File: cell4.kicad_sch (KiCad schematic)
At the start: 31 parts, among them K4 V23105A5001A201, Q12 IRLML0030, Q13 IRLML0030, SW8 SW_SPST, SW9 SW_SPST, U3 LMV324

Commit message: cell changes and fixes
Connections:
- net Batt+: now also C38.1, R62.2; no longer C39.1, R63.2
- net Batt-: now also C39.1, R63.2; no longer C38.1, R62.2
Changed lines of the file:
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@@
 	(hierarchical_label "Batt-"
 		(shape input)
-		(at 238.125 126.365 0)
+		(at 238.125 146.05 0)
 		(effects
 			(font
@@
 	(hierarchical_label "Batt+"
 		(shape input)
-		(at 238.125 146.05 0)
+		(at 238.125 126.365 0)
 		(effects
 			(font

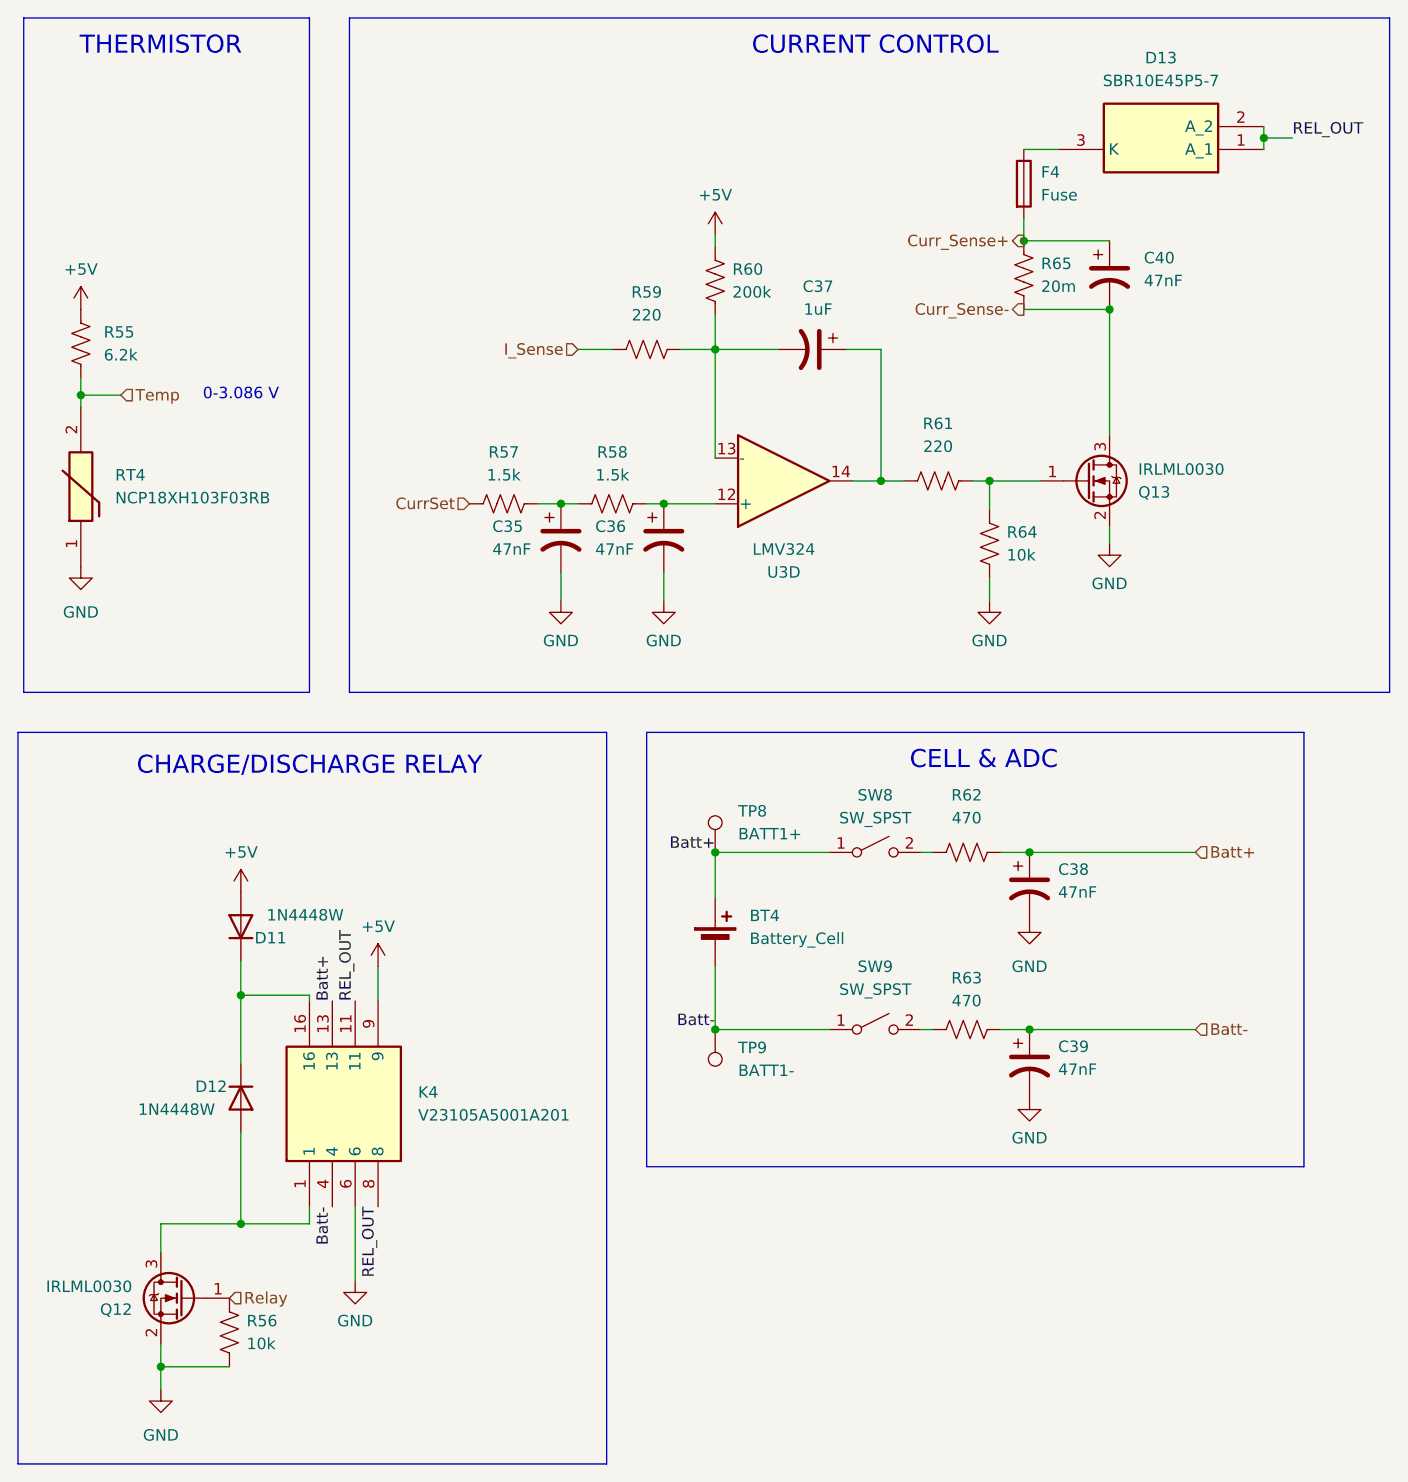
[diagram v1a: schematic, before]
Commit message: Updated current control loop hardware
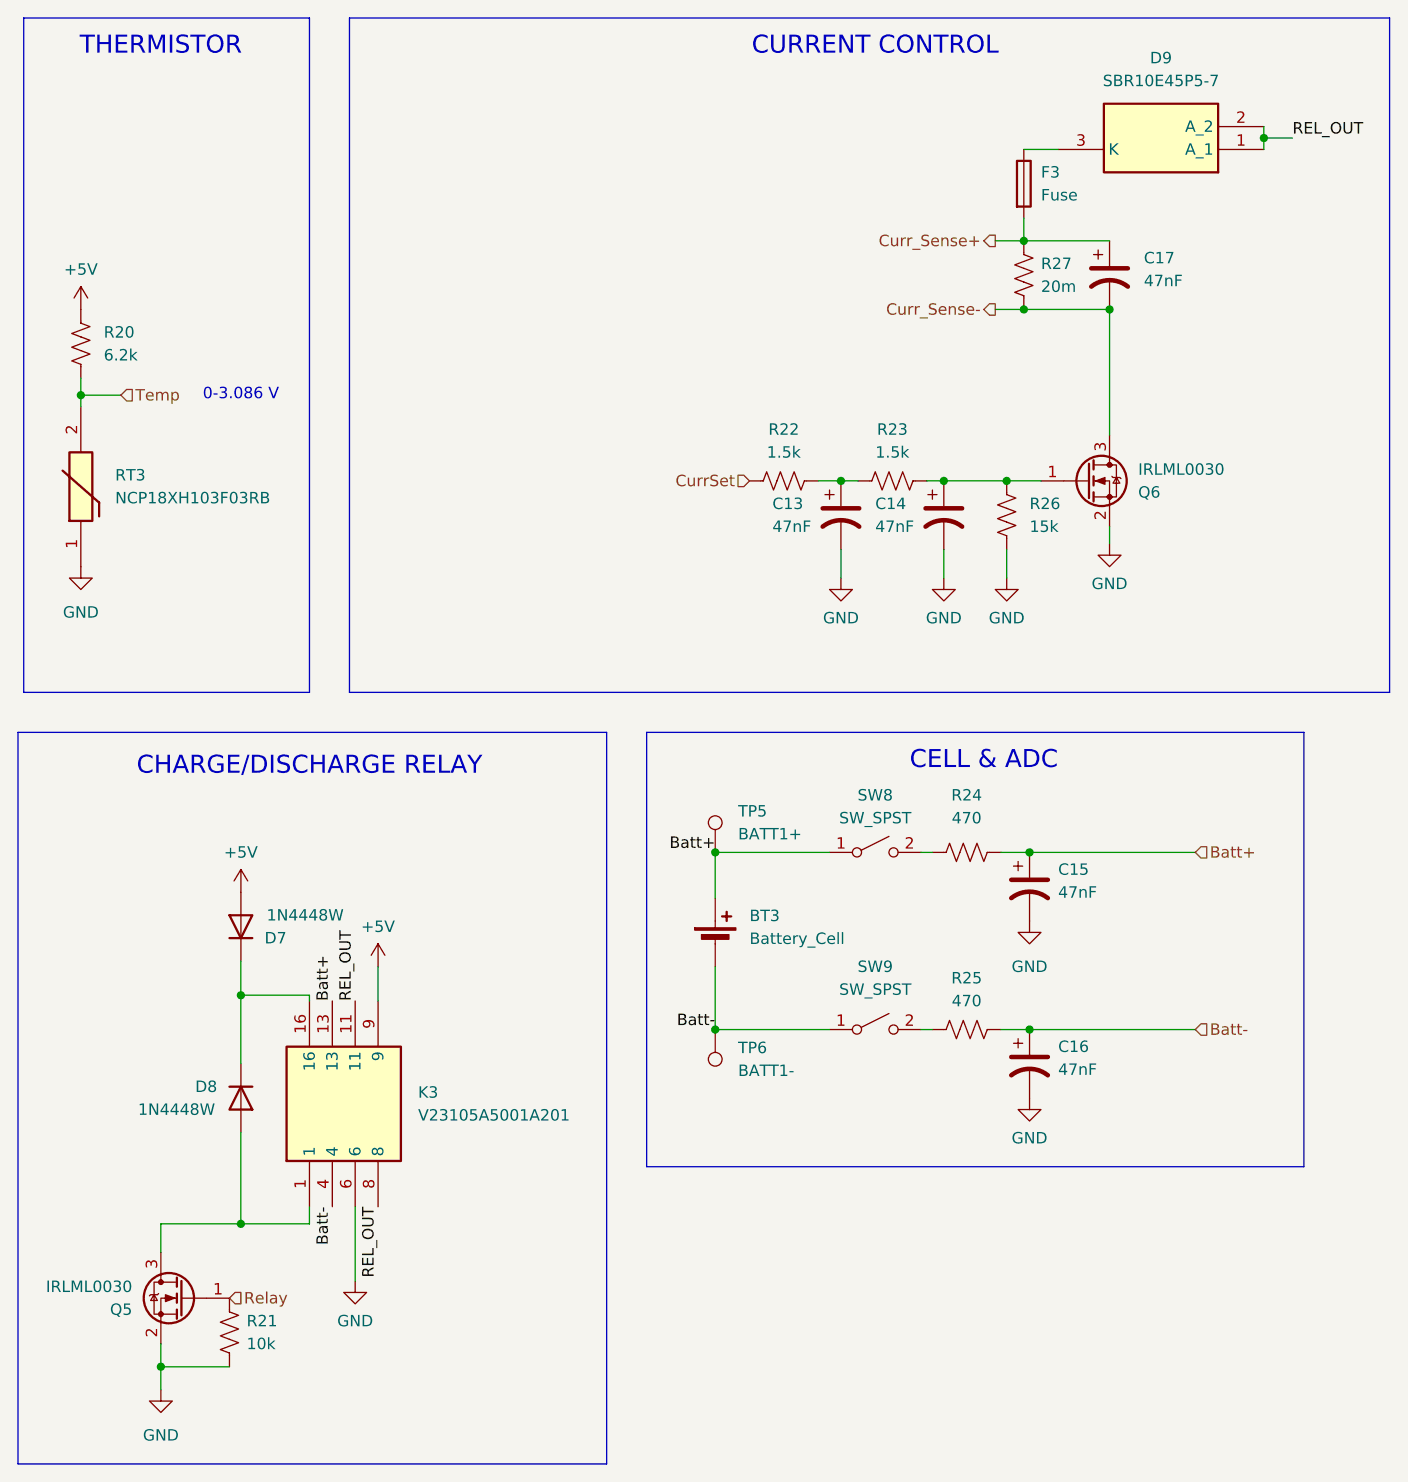
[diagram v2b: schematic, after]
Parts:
- removed BT4: Battery_Cell, symbol Device:Battery_Cell
- removed C35, C36, C38, C39, C40: 47nF, symbol Device:C_Polarized_US
- removed C37: 1uF, symbol Device:C_Polarized_US
- removed D11, D12: 1N4448W, Diode_SMD:D_SOD-123, symbol Diode:1N4448W
- removed D13: SBR10E45P5-7, SBR10E45P57, symbol SBR10E45P5-7:SBR10E45P5-7
- removed F4: Fuse, symbol Device:Fuse
- removed K4: V23105A5001A201, V23105A5001A201, symbol V23105A5001A201:V23105A5001A201
- removed Q12, Q13: IRLML0030, Package_TO_SOT_SMD:SOT-23, symbol Transistor_FET:IRLML0030
- removed R55: 6.2k, symbol Device:R_US
- removed R56, R64: 10k, symbol Device:R_US
- removed R57, R58: 1.5k, symbol Device:R_US
- removed R59, R61: 220, symbol Device:R_US
- removed R60: 200k, symbol Device:R_US
- removed R62, R63: 470, symbol Device:R_US
- removed R65: 20m, symbol Device:R_US
- removed RT4: NCP18XH103F03RB, THRMC1608X95N, symbol NCP18XH103F03RB:NCP18XH103F03RB
- removed TP8: BATT1+, symbol Connector:TestPoint
- removed TP9: BATT1-, symbol Connector:TestPoint
- removed U3: LMV324, symbol Amplifier_Operational:LMV324
- added BT3: Battery_Cell, symbol Device:Battery_Cell
- added C13, C14, C15, C16, C17: 47nF, symbol Device:C_Polarized_US
- added D7, D8: 1N4448W, Diode_SMD:D_SOD-123, symbol Diode:1N4448W
- added D9: SBR10E45P5-7, SBR10E45P57, symbol SBR10E45P5-7:SBR10E45P5-7
- added F3: Fuse, symbol Device:Fuse
- added K3: V23105A5001A201, V23105A5001A201, symbol V23105A5001A201:V23105A5001A201
- added Q5, Q6: IRLML0030, Package_TO_SOT_SMD:SOT-23, symbol Transistor_FET:IRLML0030
- added R20: 6.2k, symbol Device:R_US
- added R21: 10k, symbol Device:R_US
- added R22, R23: 1.5k, symbol Device:R_US
- added R24, R25: 470, symbol Device:R_US
- added R26: 15k, symbol Device:R_US
- added R27: 20m, symbol Device:R_US
- added RT3: NCP18XH103F03RB, THRMC1608X95N, symbol NCP18XH103F03RB:NCP18XH103F03RB
- added TP5: BATT1+, symbol Connector:TestPoint
- added TP6: BATT1-, symbol Connector:TestPoint
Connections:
- net +5V: now also D7.2 (A), K3.9, R20.1
- net Batt+: now also BT3.1 (+), C15.1, K3.13, R24.2, TP5.1
- net Batt-: now also BT3.2 (-), C16.1, K3.4, R25.2, TP6.1
- net CurrSet: now also R22.1
- net Curr_Sense+: now also C17.1, F3.2, R27.1
- net Curr_Sense-: now also C17.2, Q6.3 (D), R27.2
- net GND: now also C13.2, C14.2, C15.2, C16.2, K3.6, Q5.2 (S), Q6.2 (S), R21.2, R26.1, RT3.1
- net REL_OUT: now also D9.1 (A_1), D9.2 (A_2), K3.11, K3.8
- net Relay: now also Q5.1 (G), R21.1
- net Temp: now also R20.2, RT3.2
- net at SW9.2 (B): now also R25.1
- net at SW8.2 (B): now also R24.1
- new net: C14.1, Q6.1 (G), R23.2, R26.2
- new net: D9.3 (K), F3.1
- new net: D8.2 (A), K3.1, Q5.3 (D)
- new net: C13.1, R22.2, R23.1
- new net: D7.1 (K), D8.1 (K), K3.16

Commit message: added battery holder footprint
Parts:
- BT3: footprint (none) -> ExternalFootprints:BAT_1121
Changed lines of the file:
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@@
 	(label "REL_OUT"
 		(at 147.32 165.735 270)
-		(fields_autoplaced yes)
 		(effects
 			(font
@@
 	(label "Batt+"
 		(at 184.785 126.365 180)
-		(fields_autoplaced yes)
 		(effects
 			(font
@@
 	(label "Batt-"
 		(at 184.785 146.05 180)
-		(fields_autoplaced yes)
 		(effects
 			(font
@@
 	(label "Batt+"
 		(at 142.24 142.875 90)
-		(fields_autoplaced yes)
 		(effects
 			(font
@@
 	(label "Batt-"
 		(at 142.24 165.735 270)
-		(fields_autoplaced yes)
 		(effects
 			(font
@@
 	(label "REL_OUT"
 		(at 144.78 142.875 90)
-		(fields_autoplaced yes)
 		(effects
 			(font
@@
 	(label "REL_OUT"
 		(at 248.92 46.99 0)
-		(fields_autoplaced yes)
 		(effects
 			(font
@@
 		(shape input)
 		(at 130.81 175.895 0)
-		(fields_autoplaced yes)
 		(effects
 			(font
@@
 		(shape input)
 		(at 238.125 126.365 0)
-		(fields_autoplaced yes)
 		(effects
 			(font
@@
 		(shape output)
 		(at 215.9 58.42 180)
-		(fields_autoplaced yes)
 		(effects
 			(font
@@
 		(shape input)
 		(at 188.595 85.09 180)
-		(fields_autoplaced yes)
 		(effects
 			(font
@@
 		(shape output)
 		(at 215.9 66.04 180)
-		(fields_autoplaced yes)
 		(effects
 			(font
@@
 		(shape input)
 		(at 118.745 75.565 0)
-		(fields_autoplaced yes)
 		(effects
 			(font
@@
 		(shape input)
 		(at 238.125 146.05 0)
-		(fields_autoplaced yes)
 		(effects
 			(font
@@
 			)
 		)
-		(property "Footprint" ""
+		(property "Footprint" "ExternalFootprints:BAT_1121"
 			(at 184.785 135.001 90)
 			(effects

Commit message: All footprints assigned
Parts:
- removed SW8, SW9: SW_SPST, symbol Switch:SW_SPST
- C13, C14: value 47nF -> 0.1uF; footprint (none) -> Capacitor_SMD:C_0805_2012Metric
- C15, C16, C17: footprint (none) -> Capacitor_SMD:C_0805_2012Metric
- F3: footprint (none) -> Fuse:Fuse_1812_4532Metric
- R20, R21, R22, R23: footprint (none) -> Resistor_SMD:R_0805_2012Metric
- R24: value 470 -> 15k; footprint (none) -> Resistor_SMD:R_0805_2012Metric
- R25: value 470 -> 20m; footprint (none) -> Resistor_SMD:R_1206_3216Metric
- R26: value 15k -> 470; footprint (none) -> Resistor_SMD:R_0805_2012Metric
- R27: value 20m -> 470; footprint (none) -> Resistor_SMD:R_0805_2012Metric
- TP5, TP6: footprint (none) -> UTSVT_Special:TestPoint_HEX_3mmID
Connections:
- net Batt+: now also C16.1, R26.1, R26.2; no longer C15.1, R24.2
- net Batt-: now also C17.1, R27.1, R27.2; no longer C16.1, R25.2
- net Curr_Sense+: now also C15.1, R25.1; no longer C17.1, R27.1
- net Curr_Sense-: now also C15.2, R25.2; no longer C17.2, R27.2
- net GND: now also C17.2, R24.1; no longer C15.2, R26.1
- net at C14.1, Q6.1 (G), R23.2: now also R24.2; no longer R26.2
